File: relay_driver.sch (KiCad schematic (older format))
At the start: 7 parts, among them Q4 NMOS

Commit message: wip some layout, added a diode to watchdog power
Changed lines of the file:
@@
 AR Path="/5728BD96/57284B32" Ref="Q6"  Part="1"
 AR Path="/5736E780/57284B32" Ref="Q7"  Part="1"
-F 0 "Q5" H 4200 3100 50  0000 R CNN
+F 0 "Q7" H 4200 3100 50  0000 R CNN
 F 1 "NMOS" H 4300 3000 50  0000 R CNN
 F 2 "TO_SOT_Packages_SMD:SOT-23" H 4100 3150 50  0001 C CNN
@@
 AR Path="/5728BD96/57284C7E" Ref="R33"  Part="1"
 AR Path="/5736E780/57284C7E" Ref="R37"  Part="1"
-F 0 "R29" V 3330 3300 50  0000 C CNN
+F 0 "R37" V 3330 3300 50  0000 C CNN
 F 1 "100K" V 3250 3300 50  0000 C CNN
 F 2 "Resistors_SMD:R_0603" V 3180 3300 50  0001 C CNN
@@
 AR Path="/5728BD96/57284CE3" Ref="R32"  Part="1"
 AR Path="/5736E780/57284CE3" Ref="R36"  Part="1"
-F 0 "R28" V 3580 3050 50  0000 C CNN
+F 0 "R36" V 3580 3050 50  0000 C CNN
 F 1 "470R" V 3500 3050 50  0000 C CNN
 F 2 "Resistors_SMD:R_0603" V 3430 3050 50  0001 C CNN
@@
 AR Path="/5728BD96/5728508D" Ref="D17"  Part="1"
 AR Path="/5736E780/5728508D" Ref="D19"  Part="1"
-F 0 "D15" H 3900 2150 50  0000 C CNN
+F 0 "D19" H 3900 2150 50  0000 C CNN
 F 1 "D" H 3900 1950 50  0001 C CNN
 F 2 "Diodes_SMD:SOD-123" H 3900 2050 50  0001 C CNN
@@
 AR Path="/5728BD96/5728580D" Ref="R30"  Part="1"
 AR Path="/5736E780/5728580D" Ref="R34"  Part="1"
-F 0 "R26" V 4080 2500 50  0000 C CNN
+F 0 "R34" V 4080 2500 50  0000 C CNN
 F 1 "R" V 4000 2500 50  0001 C CNN
 F 2 "Resistors_SMD:R_1210_HandSoldering" V 3930 2500 50  0001 C CNN
@@
 AR Path="/5728BD96/573F0404" Ref="D16"  Part="1"
 AR Path="/5736E780/573F0404" Ref="D18"  Part="1"
-F 0 "D14" H 3650 1925 50  0000 L CNN
+F 0 "D18" H 3650 1925 50  0000 L CNN
 F 1 "LED" H 3650 1700 39  0000 L CNN
 F 2 "LEDs:LED_0603" V 3700 1800 50  0001 C CNN
@@
 AR Path="/5728BD96/573F0488" Ref="R31"  Part="1"
 AR Path="/5736E780/573F0488" Ref="R35"  Part="1"
-F 0 "R27" V 3830 2750 50  0000 C CNN
+F 0 "R35" V 3830 2750 50  0000 C CNN
 F 1 "2K" V 3750 2750 50  0000 C CNN
 F 2 "Resistors_SMD:R_0603" V 3680 2750 50  0001 C CNN

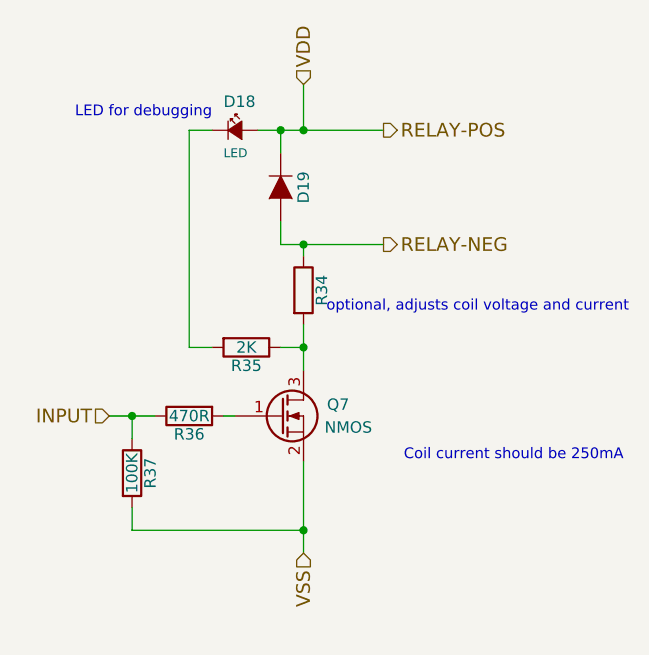
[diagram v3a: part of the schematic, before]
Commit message: got rid of isometer connector
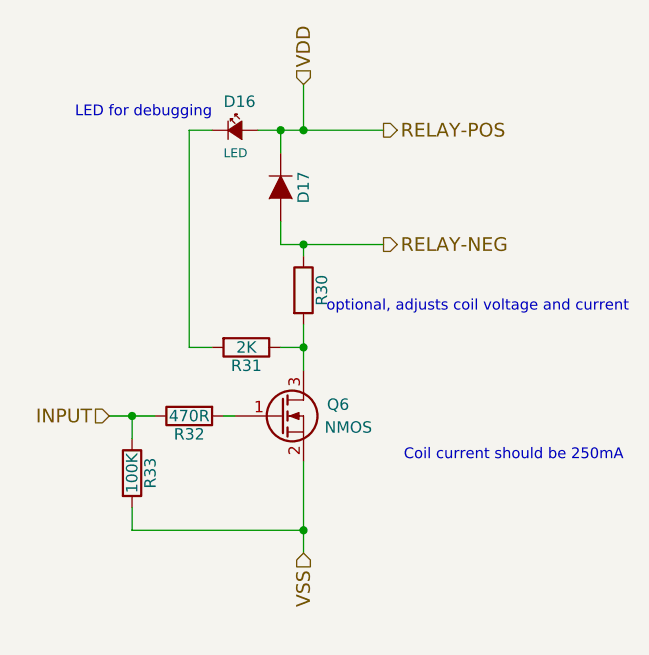
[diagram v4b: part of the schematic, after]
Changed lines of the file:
@@
 AR Path="/5728BD96/57284B32" Ref="Q6"  Part="1"
 AR Path="/5736E780/57284B32" Ref="Q7"  Part="1"
-F 0 "Q7" H 4200 3100 50  0000 R CNN
+F 0 "Q6" H 4200 3100 50  0000 R CNN
 F 1 "NMOS" H 4300 3000 50  0000 R CNN
 F 2 "TO_SOT_Packages_SMD:SOT-23" H 4100 3150 50  0001 C CNN
@@
 AR Path="/5728BD96/57284C7E" Ref="R33"  Part="1"
 AR Path="/5736E780/57284C7E" Ref="R37"  Part="1"
-F 0 "R37" V 3330 3300 50  0000 C CNN
+F 0 "R33" V 3330 3300 50  0000 C CNN
 F 1 "100K" V 3250 3300 50  0000 C CNN
 F 2 "Resistors_SMD:R_0603" V 3180 3300 50  0001 C CNN
@@
 AR Path="/5728BD96/57284CE3" Ref="R32"  Part="1"
 AR Path="/5736E780/57284CE3" Ref="R36"  Part="1"
-F 0 "R36" V 3580 3050 50  0000 C CNN
+F 0 "R32" V 3580 3050 50  0000 C CNN
 F 1 "470R" V 3500 3050 50  0000 C CNN
 F 2 "Resistors_SMD:R_0603" V 3430 3050 50  0001 C CNN
@@
 AR Path="/5728BD96/5728508D" Ref="D17"  Part="1"
 AR Path="/5736E780/5728508D" Ref="D19"  Part="1"
-F 0 "D19" H 3900 2150 50  0000 C CNN
+F 0 "D17" H 3900 2150 50  0000 C CNN
 F 1 "D" H 3900 1950 50  0001 C CNN
 F 2 "Diodes_SMD:SOD-123" H 3900 2050 50  0001 C CNN
@@
 AR Path="/5728BD96/5728580D" Ref="R30"  Part="1"
 AR Path="/5736E780/5728580D" Ref="R34"  Part="1"
-F 0 "R34" V 4080 2500 50  0000 C CNN
+F 0 "R30" V 4080 2500 50  0000 C CNN
 F 1 "R" V 4000 2500 50  0001 C CNN
 F 2 "Resistors_SMD:R_1210_HandSoldering" V 3930 2500 50  0001 C CNN
@@
 AR Path="/5728BD96/573F0404" Ref="D16"  Part="1"
 AR Path="/5736E780/573F0404" Ref="D18"  Part="1"
-F 0 "D18" H 3650 1925 50  0000 L CNN
+F 0 "D16" H 3650 1925 50  0000 L CNN
 F 1 "LED" H 3650 1700 39  0000 L CNN
 F 2 "LEDs:LED_0603" V 3700 1800 50  0001 C CNN
@@
 AR Path="/5728BD96/573F0488" Ref="R31"  Part="1"
 AR Path="/5736E780/573F0488" Ref="R35"  Part="1"
-F 0 "R35" V 3830 2750 50  0000 C CNN
+F 0 "R31" V 3830 2750 50  0000 C CNN
 F 1 "2K" V 3750 2750 50  0000 C CNN
 F 2 "Resistors_SMD:R_0603" V 3680 2750 50  0001 C CNN

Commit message: reordered all reference designators
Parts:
- renumbered D12 to D10, D13 to D11, R22 to R21, R23 to R22, R24 to R23, R25 to R24
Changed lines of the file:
@@
 AR Path="/5728BD96/57284B32" Ref="Q6"  Part="1"
 AR Path="/5736E780/57284B32" Ref="Q7"  Part="1"
-F 0 "Q6" H 4200 3100 50  0000 R CNN
+F 0 "Q7" H 4200 3100 50  0000 R CNN
 F 1 "NMOS" H 4300 3000 50  0000 R CNN
 F 2 "TO_SOT_Packages_SMD:SOT-23" H 4100 3150 50  0001 C CNN
@@
 $EndComp
 $Comp
-L R R25
+L R R24
 U 1 1 57284C7E
 P 3250 3300
-AR Path="/572843F5/57284C7E" Ref="R25"  Part="1"
-AR Path="/5728B2EB/57284C7E" Ref="R29"  Part="1"
-AR Path="/5728BD96/57284C7E" Ref="R33"  Part="1"
-AR Path="/5736E780/57284C7E" Ref="R37"  Part="1"
-F 0 "R33" V 3330 3300 50  0000 C CNN
+AR Path="/572843F5/57284C7E" Ref="R24"  Part="1"
+AR Path="/5728B2EB/57284C7E" Ref="R28"  Part="1"
+AR Path="/5728BD96/57284C7E" Ref="R32"  Part="1"
+AR Path="/5736E780/57284C7E" Ref="R36"  Part="1"
+F 0 "R36" V 3330 3300 50  0000 C CNN
 F 1 "100K" V 3250 3300 50  0000 C CNN
 F 2 "Resistors_SMD:R_0603" V 3180 3300 50  0001 C CNN
@@
 $EndComp
 $Comp
-L R R24
+L R R23
 U 1 1 57284CE3
 P 3500 3050
-AR Path="/572843F5/57284CE3" Ref="R24"  Part="1"
-AR Path="/5728B2EB/57284CE3" Ref="R28"  Part="1"
-AR Path="/5728BD96/57284CE3" Ref="R32"  Part="1"
-AR Path="/5736E780/57284CE3" Ref="R36"  Part="1"
-F 0 "R32" V 3580 3050 50  0000 C CNN
+AR Path="/572843F5/57284CE3" Ref="R23"  Part="1"
+AR Path="/5728B2EB/57284CE3" Ref="R27"  Part="1"
+AR Path="/5728BD96/57284CE3" Ref="R31"  Part="1"
+AR Path="/5736E780/57284CE3" Ref="R35"  Part="1"
+F 0 "R35" V 3580 3050 50  0000 C CNN
 F 1 "470R" V 3500 3050 50  0000 C CNN
 F 2 "Resistors_SMD:R_0603" V 3430 3050 50  0001 C CNN
@@
 $EndComp
 $Comp
-L D D13
+L D D11
 U 1 1 5728508D
 P 3900 2050
-AR Path="/572843F5/5728508D" Ref="D13"  Part="1"
-AR Path="/5728B2EB/5728508D" Ref="D15"  Part="1"
-AR Path="/5728BD96/5728508D" Ref="D17"  Part="1"
-AR Path="/5736E780/5728508D" Ref="D19"  Part="1"
+AR Path="/572843F5/5728508D" Ref="D11"  Part="1"
+AR Path="/5728B2EB/5728508D" Ref="D13"  Part="1"
+AR Path="/5728BD96/5728508D" Ref="D15"  Part="1"
+AR Path="/5736E780/5728508D" Ref="D17"  Part="1"
 F 0 "D17" H 3900 2150 50  0000 C CNN
 F 1 "D" H 3900 1950 50  0001 C CNN
@@
 	3900 1900 3900 1800
 $Comp
-L R R22
+L R R21
 U 1 1 5728580D
 P 4000 2500
-AR Path="/572843F5/5728580D" Ref="R22"  Part="1"
-AR Path="/5728B2EB/5728580D" Ref="R26"  Part="1"
-AR Path="/5728BD96/5728580D" Ref="R30"  Part="1"
-AR Path="/5736E780/5728580D" Ref="R34"  Part="1"
-F 0 "R30" V 4080 2500 50  0000 C CNN
+AR Path="/572843F5/5728580D" Ref="R21"  Part="1"
+AR Path="/5728B2EB/5728580D" Ref="R25"  Part="1"
+AR Path="/5728BD96/5728580D" Ref="R29"  Part="1"
+AR Path="/5736E780/5728580D" Ref="R33"  Part="1"
+F 0 "R33" V 4080 2500 50  0000 C CNN
 F 1 "R" V 4000 2500 50  0001 C CNN
 F 2 "Resistors_SMD:R_1210_HandSoldering" V 3930 2500 50  0001 C CNN
@@
 Connection ~ 4000 1800
 $Comp
-L Led_Small D12
+L Led_Small D10
 U 1 1 573F0404
 P 3700 1800
-AR Path="/572843F5/573F0404" Ref="D12"  Part="1"
-AR Path="/5728B2EB/573F0404" Ref="D14"  Part="1"
-AR Path="/5728BD96/573F0404" Ref="D16"  Part="1"
-AR Path="/5736E780/573F0404" Ref="D18"  Part="1"
+AR Path="/572843F5/573F0404" Ref="D10"  Part="1"
+AR Path="/5728B2EB/573F0404" Ref="D12"  Part="1"
+AR Path="/5728BD96/573F0404" Ref="D14"  Part="1"
+AR Path="/5736E780/573F0404" Ref="D16"  Part="1"
 F 0 "D16" H 3650 1925 50  0000 L CNN
 F 1 "LED" H 3650 1700 39  0000 L CNN
@@
 $EndComp
 $Comp
-L R R23
+L R R22
 U 1 1 573F0488
 P 3750 2750
-AR Path="/572843F5/573F0488" Ref="R23"  Part="1"
-AR Path="/5728B2EB/573F0488" Ref="R27"  Part="1"
-AR Path="/5728BD96/573F0488" Ref="R31"  Part="1"
-AR Path="/5736E780/573F0488" Ref="R35"  Part="1"
-F 0 "R31" V 3830 2750 50  0000 C CNN
+AR Path="/572843F5/573F0488" Ref="R22"  Part="1"
+AR Path="/5728B2EB/573F0488" Ref="R26"  Part="1"
+AR Path="/5728BD96/573F0488" Ref="R30"  Part="1"
+AR Path="/5736E780/573F0488" Ref="R34"  Part="1"
+F 0 "R34" V 3830 2750 50  0000 C CNN
 F 1 "2K" V 3750 2750 50  0000 C CNN
 F 2 "Resistors_SMD:R_0603" V 3680 2750 50  0001 C CNN
